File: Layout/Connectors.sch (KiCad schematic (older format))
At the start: 3 parts

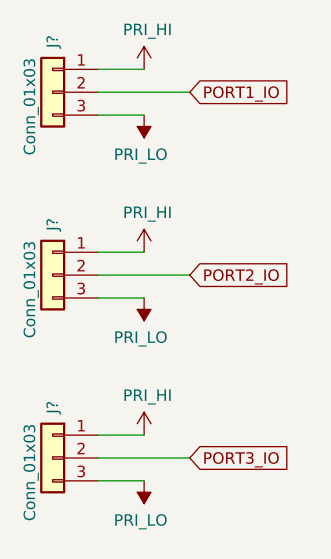
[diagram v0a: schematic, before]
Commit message: Add more sheets. Add LEDs
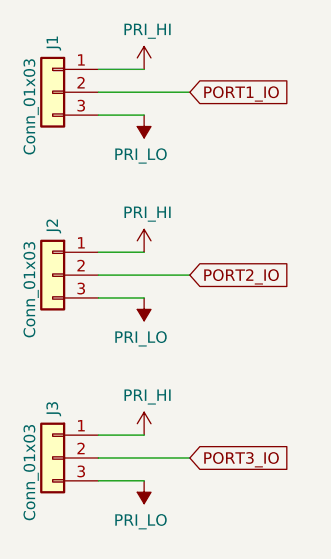
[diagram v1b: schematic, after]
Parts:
- gave numbers to parts that had none: 3
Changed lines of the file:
@@
 $Descr A4 11693 8268
 encoding utf-8
-Sheet 3 4
+Sheet 3 7
 Title ""
 Date ""
@@
 U 1 1 5F383B41
 P 2350 2100
-F 0 "J?" V 2350 2350 50  0000 R CNN
+AR Path="/5F383B41" Ref="J?"  Part="1"
+AR Path="/5F3717FF/5F383B41" Ref="J1"  Part="1"
+F 0 "J1" V 2350 2350 50  0000 R CNN
 F 1 "Conn_01x03" V 2450 2250 50  0000 R CNN
 F 2 "" H 2350 2100 50  0001 C CNN
@@
 U 1 1 5F383B47
 P 2350 2900
-F 0 "J?" V 2350 3150 50  0000 R CNN
+AR Path="/5F383B47" Ref="J?"  Part="1"
+AR Path="/5F3717FF/5F383B47" Ref="J2"  Part="1"
+F 0 "J2" V 2350 3150 50  0000 R CNN
 F 1 "Conn_01x03" V 2450 3050 50  0000 R CNN
 F 2 "" H 2350 2900 50  0001 C CNN
@@
 U 1 1 5F383B4D
 P 2350 3700
-F 0 "J?" V 2350 3950 50  0000 R CNN
+AR Path="/5F383B4D" Ref="J?"  Part="1"
+AR Path="/5F3717FF/5F383B4D" Ref="J3"  Part="1"
+F 0 "J3" V 2350 3950 50  0000 R CNN
 F 1 "Conn_01x03" V 2450 3850 50  0000 R CNN
 F 2 "" H 2350 3700 50  0001 C CNN
@@
 P 2750 2800
 AR Path="/5F383B59" Ref="#PWR?"  Part="1"
-AR Path="/5F3717FF/5F383B59" Ref="#PWR?"  Part="1"
-F 0 "#PWR?" H 2750 2650 50  0001 C CNN
+AR Path="/5F3717FF/5F383B59" Ref="#PWR0108"  Part="1"
+F 0 "#PWR0108" H 2750 2650 50  0001 C CNN
 F 1 "PRI_HI" H 2765 2973 50  0000 C CNN
 F 2 "" H 2750 2800 50  0001 C CNN
@@
 P 2750 3600
 AR Path="/5F383B5F" Ref="#PWR?"  Part="1"
-AR Path="/5F3717FF/5F383B5F" Ref="#PWR?"  Part="1"
-F 0 "#PWR?" H 2750 3450 50  0001 C CNN
+AR Path="/5F3717FF/5F383B5F" Ref="#PWR0109"  Part="1"
+F 0 "#PWR0109" H 2750 3450 50  0001 C CNN
 F 1 "PRI_HI" H 2765 3773 50  0000 C CNN
 F 2 "" H 2750 3600 50  0001 C CNN
@@
 P 2750 2200
 AR Path="/5F383B65" Ref="#PWR?"  Part="1"
-AR Path="/5F3717FF/5F383B65" Ref="#PWR?"  Part="1"
-F 0 "#PWR?" H 2750 2050 50  0001 C CNN
+AR Path="/5F3717FF/5F383B65" Ref="#PWR0110"  Part="1"
+F 0 "#PWR0110" H 2750 2050 50  0001 C CNN
 F 1 "PRI_LO" H 2765 2373 50  0000 C CNN
 F 2 "" H 2750 2200 50  0001 C CNN
@@
 P 2750 3000
 AR Path="/5F383B6B" Ref="#PWR?"  Part="1"
-AR Path="/5F3717FF/5F383B6B" Ref="#PWR?"  Part="1"
-F 0 "#PWR?" H 2750 2850 50  0001 C CNN
+AR Path="/5F3717FF/5F383B6B" Ref="#PWR0111"  Part="1"
+F 0 "#PWR0111" H 2750 2850 50  0001 C CNN
 F 1 "PRI_LO" H 2765 3173 50  0000 C CNN
 F 2 "" H 2750 3000 50  0001 C CNN
@@
 P 2750 3800
 AR Path="/5F383B71" Ref="#PWR?"  Part="1"
-AR Path="/5F3717FF/5F383B71" Ref="#PWR?"  Part="1"
-F 0 "#PWR?" H 2750 3650 50  0001 C CNN
+AR Path="/5F3717FF/5F383B71" Ref="#PWR0112"  Part="1"
+F 0 "#PWR0112" H 2750 3650 50  0001 C CNN
 F 1 "PRI_LO" H 2765 3973 50  0000 C CNN
 F 2 "" H 2750 3800 50  0001 C CNN
@@
 P 2750 2000
 AR Path="/5F383B53" Ref="#PWR?"  Part="1"
-AR Path="/5F3717FF/5F383B53" Ref="#PWR?"  Part="1"
-F 0 "#PWR?" H 2750 1850 50  0001 C CNN
+AR Path="/5F3717FF/5F383B53" Ref="#PWR0113"  Part="1"
+F 0 "#PWR0113" H 2750 1850 50  0001 C CNN
 F 1 "PRI_HI" H 2765 2173 50  0000 C CNN
 F 2 "" H 2750 2000 50  0001 C CNN

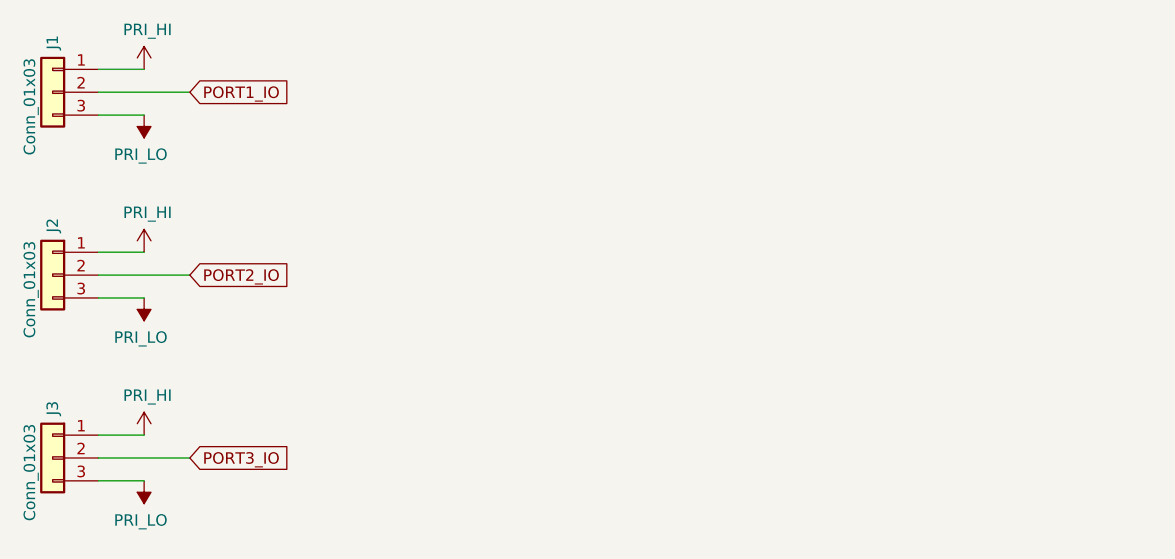
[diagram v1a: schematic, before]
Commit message: Add programming header
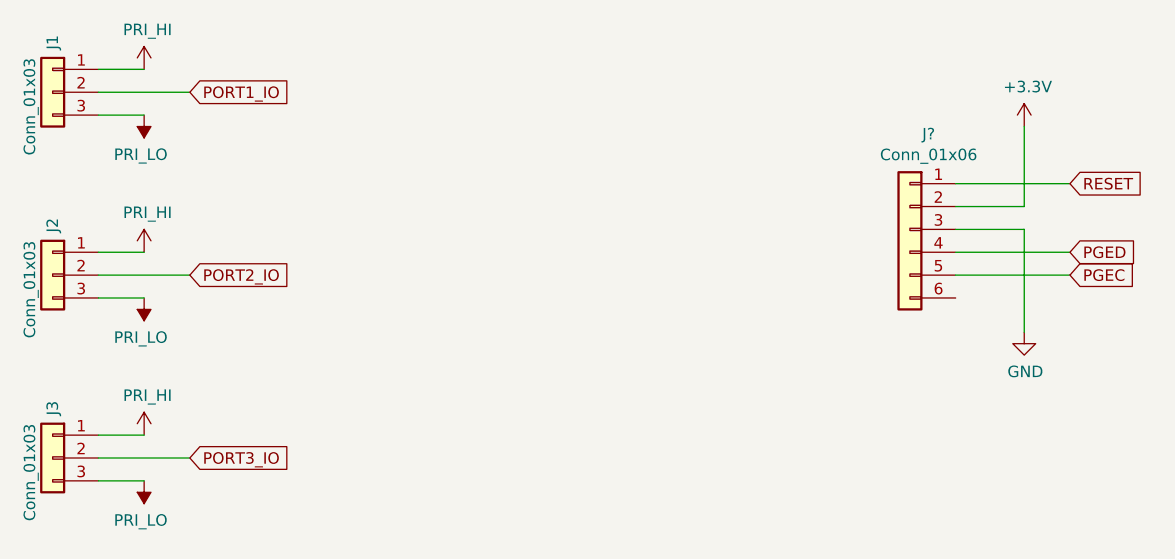
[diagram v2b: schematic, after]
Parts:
- added J?: Conn_01x06, symbol Connector_Generic:Conn_01x06
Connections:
- new net +3V3: J?.2 (Pin_2)
- new net GND: J?.3 (Pin_3)
- new net PGEC: J?.5 (Pin_5)
- new net PGED: J?.4 (Pin_4)
- new net RESET: J?.1 (Pin_1)
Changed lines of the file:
@@
 Wire Wire Line
 	2550 2100 2950 2100
+$Comp
+L Connector_Generic:Conn_01x06 J?
+U 1 1 5F395426
+P 6100 2700
+F 0 "J?" H 6018 3117 50  0000 C CNN
+F 1 "Conn_01x06" H 6018 3026 50  0000 C CNN
+F 2 "" H 6100 2700 50  0001 C CNN
+F 3 "~" H 6100 2700 50  0001 C CNN
+	1    6100 2700
+	-1   0    0    -1
+$EndComp
+Text GLabel 6800 2500 2    50   Input ~ 0
+RESET
+Text GLabel 6800 2800 2    50   Input ~ 0
+PGED
+Text GLabel 6800 2900 2    50   Input ~ 0
+PGEC
+Wire Wire Line
+	6300 2500 6800 2500
+Wire Wire Line
+	6300 2800 6800 2800
+Wire Wire Line
+	6300 2900 6800 2900
+$Comp
+L power:+3.3V #PWR?
+U 1 1 5F3966ED
+P 6600 2250
+F 0 "#PWR?" H 6600 2100 50  0001 C CNN
+F 1 "+3.3V" H 6615 2423 50  0000 C CNN
+F 2 "" H 6600 2250 50  0001 C CNN
+F 3 "" H 6600 2250 50  0001 C CNN
+	1    6600 2250
+	1    0    0    -1
+$EndComp
+$Comp
+L power:GND #PWR?
+U 1 1 5F396E80
+P 6600 3150
+F 0 "#PWR?" H 6600 2900 50  0001 C CNN
+F 1 "GND" H 6605 2977 50  0000 C CNN
+F 2 "" H 6600 3150 50  0001 C CNN
+F 3 "" H 6600 3150 50  0001 C CNN
+	1    6600 3150
+	1    0    0    -1
+$EndComp
+Wire Wire Line
+	6300 2600 6600 2600
+Wire Wire Line
+	6600 2600 6600 2250
+Wire Wire Line
+	6300 2700 6600 2700
+Wire Wire Line
+	6600 2700 6600 3150
 $EndSCHEMATC

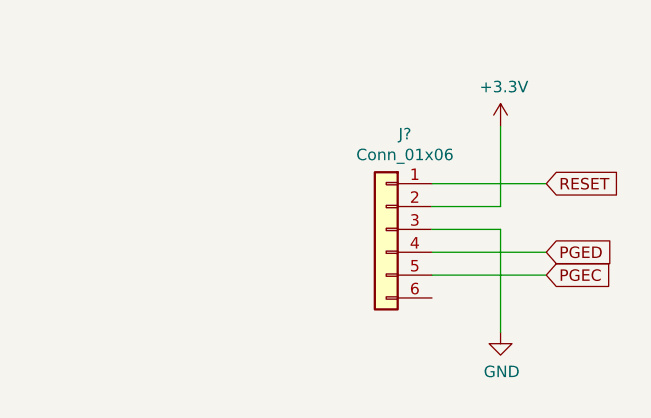
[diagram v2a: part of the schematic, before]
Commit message: Update footprints and references
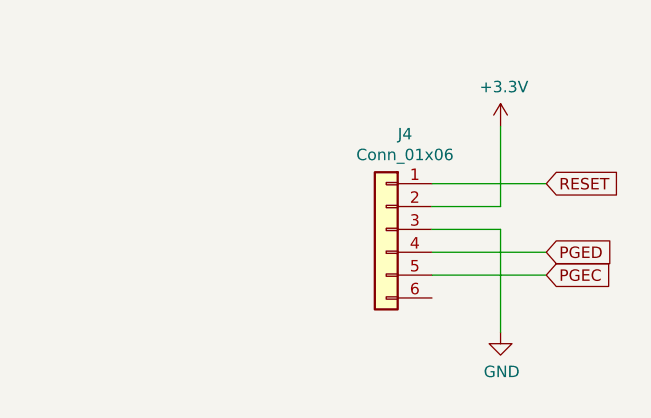
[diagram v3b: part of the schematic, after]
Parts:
- J1, J2, J3: footprint (none) -> Connector_PinHeader_1.00mm:PinHeader_1x03_P1.00mm_Vertical
- J4: renamed from J?; footprint (none) -> Connector_PinHeader_1.00mm:PinHeader_1x06_P1.00mm_Vertical
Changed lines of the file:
@@
 F 0 "J1" V 2350 2350 50  0000 R CNN
 F 1 "Conn_01x03" V 2450 2250 50  0000 R CNN
-F 2 "" H 2350 2100 50  0001 C CNN
+F 2 "Connector_PinHeader_1.00mm:PinHeader_1x03_P1.00mm_Vertical" H 2350 2100 50  0001 C CNN
 F 3 "~" H 2350 2100 50  0001 C CNN
 	1    2350 2100
@@
 F 0 "J2" V 2350 3150 50  0000 R CNN
 F 1 "Conn_01x03" V 2450 3050 50  0000 R CNN
-F 2 "" H 2350 2900 50  0001 C CNN
+F 2 "Connector_PinHeader_1.00mm:PinHeader_1x03_P1.00mm_Vertical" H 2350 2900 50  0001 C CNN
 F 3 "~" H 2350 2900 50  0001 C CNN
 	1    2350 2900
@@
 F 0 "J3" V 2350 3950 50  0000 R CNN
 F 1 "Conn_01x03" V 2450 3850 50  0000 R CNN
-F 2 "" H 2350 3700 50  0001 C CNN
+F 2 "Connector_PinHeader_1.00mm:PinHeader_1x03_P1.00mm_Vertical" H 2350 3700 50  0001 C CNN
 F 3 "~" H 2350 3700 50  0001 C CNN
 	1    2350 3700
@@
 	2550 2100 2950 2100
 $Comp
-L Connector_Generic:Conn_01x06 J?
+L Connector_Generic:Conn_01x06 J4
 U 1 1 5F395426
 P 6100 2700
-F 0 "J?" H 6018 3117 50  0000 C CNN
+F 0 "J4" H 6018 3117 50  0000 C CNN
 F 1 "Conn_01x06" H 6018 3026 50  0000 C CNN
-F 2 "" H 6100 2700 50  0001 C CNN
+F 2 "Connector_PinHeader_1.00mm:PinHeader_1x06_P1.00mm_Vertical" H 6100 2700 50  0001 C CNN
 F 3 "~" H 6100 2700 50  0001 C CNN
 	1    6100 2700
@@
 	6300 2900 6800 2900
 $Comp
-L power:+3.3V #PWR?
+L power:+3.3V #PWR0117
 U 1 1 5F3966ED
 P 6600 2250
-F 0 "#PWR?" H 6600 2100 50  0001 C CNN
+F 0 "#PWR0117" H 6600 2100 50  0001 C CNN
 F 1 "+3.3V" H 6615 2423 50  0000 C CNN
 F 2 "" H 6600 2250 50  0001 C CNN
@@
 $EndComp
 $Comp
-L power:GND #PWR?
+L power:GND #PWR0118
 U 1 1 5F396E80
 P 6600 3150
-F 0 "#PWR?" H 6600 2900 50  0001 C CNN
+F 0 "#PWR0118" H 6600 2900 50  0001 C CNN
 F 1 "GND" H 6605 2977 50  0000 C CNN
 F 2 "" H 6600 3150 50  0001 C CNN

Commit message: Fix connector footprint
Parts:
- J1, J2, J3: footprint Connector_PinHeader_1.00mm:PinHeader_1x03_P1.00mm_Vertical -> Connector_PinHeader_2.54mm:PinHeader_1x03_P2.54mm_Vertical
- J4: footprint Connector_PinHeader_1.00mm:PinHeader_1x06_P1.00mm_Vertical -> Connector_PinHeader_2.54mm:PinHeader_1x06_P2.54mm_Vertical
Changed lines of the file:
@@
 F 0 "J1" V 2350 2350 50  0000 R CNN
 F 1 "Conn_01x03" V 2450 2250 50  0000 R CNN
-F 2 "Connector_PinHeader_1.00mm:PinHeader_1x03_P1.00mm_Vertical" H 2350 2100 50  0001 C CNN
+F 2 "Connector_PinHeader_2.54mm:PinHeader_1x03_P2.54mm_Vertical" H 2350 2100 50  0001 C CNN
 F 3 "~" H 2350 2100 50  0001 C CNN
 	1    2350 2100
@@
 F 0 "J2" V 2350 3150 50  0000 R CNN
 F 1 "Conn_01x03" V 2450 3050 50  0000 R CNN
-F 2 "Connector_PinHeader_1.00mm:PinHeader_1x03_P1.00mm_Vertical" H 2350 2900 50  0001 C CNN
+F 2 "Connector_PinHeader_2.54mm:PinHeader_1x03_P2.54mm_Vertical" H 2350 2900 50  0001 C CNN
 F 3 "~" H 2350 2900 50  0001 C CNN
 	1    2350 2900
@@
 F 0 "J3" V 2350 3950 50  0000 R CNN
 F 1 "Conn_01x03" V 2450 3850 50  0000 R CNN
-F 2 "Connector_PinHeader_1.00mm:PinHeader_1x03_P1.00mm_Vertical" H 2350 3700 50  0001 C CNN
+F 2 "Connector_PinHeader_2.54mm:PinHeader_1x03_P2.54mm_Vertical" H 2350 3700 50  0001 C CNN
 F 3 "~" H 2350 3700 50  0001 C CNN
 	1    2350 3700
@@
 F 0 "J4" H 6018 3117 50  0000 C CNN
 F 1 "Conn_01x06" H 6018 3026 50  0000 C CNN
-F 2 "Connector_PinHeader_1.00mm:PinHeader_1x06_P1.00mm_Vertical" H 6100 2700 50  0001 C CNN
+F 2 "Connector_PinHeader_2.54mm:PinHeader_1x06_P2.54mm_Vertical" H 6100 2700 50  0001 C CNN
 F 3 "~" H 6100 2700 50  0001 C CNN
 	1    6100 2700

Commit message: Layout
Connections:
- net PORT1_IO: now also J1.3 (Pin_3); no longer J1.2 (Pin_2)
- net PORT2_IO: now also J2.3 (Pin_3); no longer J2.2 (Pin_2)
- net PORT3_IO: now also J3.3 (Pin_3); no longer J3.2 (Pin_2)
- net PRI_LO: now also J1.2 (Pin_2), J2.2 (Pin_2), J3.2 (Pin_2); no longer J1.3 (Pin_3), J2.3 (Pin_3), J3.3 (Pin_3)
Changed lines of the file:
@@
 L power:PRI_LO #PWR?
 U 1 1 5F383B65
-P 2750 2200
+P 3050 2000
 AR Path="/5F383B65" Ref="#PWR?"  Part="1"
 AR Path="/5F3717FF/5F383B65" Ref="#PWR0110"  Part="1"
-F 0 "#PWR0110" H 2750 2050 50  0001 C CNN
-F 1 "PRI_LO" H 2765 2373 50  0000 C CNN
-F 2 "" H 2750 2200 50  0001 C CNN
-F 3 "" H 2750 2200 50  0001 C CNN
-	1    2750 2200
-	-1   0    0    1
+F 0 "#PWR0110" H 3050 1850 50  0001 C CNN
+F 1 "PRI_LO" H 3065 2173 50  0000 C CNN
+F 2 "" H 3050 2000 50  0001 C CNN
+F 3 "" H 3050 2000 50  0001 C CNN
+	1    3050 2000
+	1    0    0    -1
 $EndComp
 $Comp
 L power:PRI_LO #PWR?
 U 1 1 5F383B6B
-P 2750 3000
+P 3050 2800
 AR Path="/5F383B6B" Ref="#PWR?"  Part="1"
 AR Path="/5F3717FF/5F383B6B" Ref="#PWR0111"  Part="1"
-F 0 "#PWR0111" H 2750 2850 50  0001 C CNN
-F 1 "PRI_LO" H 2765 3173 50  0000 C CNN
-F 2 "" H 2750 3000 50  0001 C CNN
-F 3 "" H 2750 3000 50  0001 C CNN
-	1    2750 3000
-	-1   0    0    1
+F 0 "#PWR0111" H 3050 2650 50  0001 C CNN
+F 1 "PRI_LO" H 3065 2973 50  0000 C CNN
+F 2 "" H 3050 2800 50  0001 C CNN
+F 3 "" H 3050 2800 50  0001 C CNN
+	1    3050 2800
+	1    0    0    -1
 $EndComp
 $Comp
 L power:PRI_LO #PWR?
 U 1 1 5F383B71
-P 2750 3800
+P 3050 3600
 AR Path="/5F383B71" Ref="#PWR?"  Part="1"
 AR Path="/5F3717FF/5F383B71" Ref="#PWR0112"  Part="1"
-F 0 "#PWR0112" H 2750 3650 50  0001 C CNN
-F 1 "PRI_LO" H 2765 3973 50  0000 C CNN
-F 2 "" H 2750 3800 50  0001 C CNN
-F 3 "" H 2750 3800 50  0001 C CNN
-	1    2750 3800
-	-1   0    0    1
+F 0 "#PWR0112" H 3050 3450 50  0001 C CNN
+F 1 "PRI_LO" H 3065 3773 50  0000 C CNN
+F 2 "" H 3050 3600 50  0001 C CNN
+F 3 "" H 3050 3600 50  0001 C CNN
+	1    3050 3600
+	1    0    0    -1
 $EndComp
 Wire Wire Line
@@
 	1    0    0    -1
 $EndComp
-Wire Wire Line
-	2550 3000 2750 3000
-Wire Wire Line
-	2550 3800 2750 3800
-Wire Wire Line
-	2550 2200 2750 2200
-Text GLabel 2950 2100 2    50   Input ~ 0
+Text GLabel 2700 2200 2    50   Input ~ 0
 PORT1_IO
-Text GLabel 2950 2900 2    50   Input ~ 0
+Text GLabel 2700 3000 2    50   Input ~ 0
 PORT2_IO
-Text GLabel 2950 3700 2    50   Input ~ 0
+Text GLabel 2700 3800 2    50   Input ~ 0
 PORT3_IO
-Wire Wire Line
-	2550 3700 2950 3700
-Wire Wire Line
-	2550 2900 2950 2900
-Wire Wire Line
-	2550 2100 2950 2100
 $Comp
 L Connector_Generic:Conn_01x06 J4
@@
 Wire Wire Line
 	6600 2700 6600 3150
+Wire Wire Line
+	2550 2200 2700 2200
+Wire Wire Line
+	2550 2100 3050 2100
+Wire Wire Line
+	3050 2100 3050 2000
+Wire Wire Line
+	2700 3000 2550 3000
+Wire Wire Line
+	2550 2900 3050 2900
+Wire Wire Line
+	3050 2900 3050 2800
+Wire Wire Line
+	2550 3800 2700 3800
+Wire Wire Line
+	2550 3700 3050 3700
+Wire Wire Line
+	3050 3700 3050 3600
 $EndSCHEMATC
